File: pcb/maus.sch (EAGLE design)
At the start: 87 parts, among them IC1 AD712R, Q1 BSS123, Q2 BSS123, Q3 BSS123, Q4 BSS123, Q5 BSS123, U1 ESP32-S2-WROOM, U2 CH340C, U3 CP2102, U4 LP3965EMP-3.3, U5 LSM9DS1TR

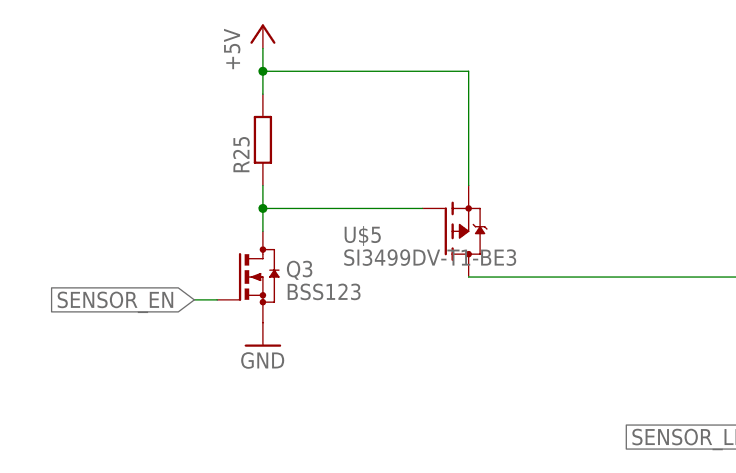
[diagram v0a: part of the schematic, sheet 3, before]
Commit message: fixed mosfet part prefix
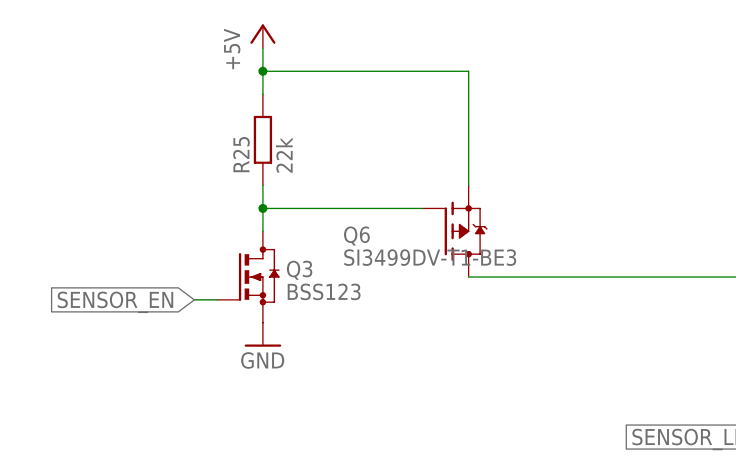
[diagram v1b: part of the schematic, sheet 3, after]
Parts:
- removed U$5, U$6: SI3499DV-T1-BE3, mosfet:SI3499DV-T1-BE3
- added Q6, Q7: SI3499DV-T1-BE3, mosfet:SI3499DV-T1-BE3
- R25: value (none) -> 22k
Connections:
- net +5V: now also Q6.S, Q7.S; no longer U$5.S, U$6.S
- net /VBUS_EN: now also Q7.G; no longer U$6.G
- net N$2: now also Q6.G; no longer U$5.G
- net N$7: now also Q6.D; no longer U$5.D
- net USB_VBUS: now also Q7.D; no longer U$6.D
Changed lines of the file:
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@@
 <part name="Q5" library="transistor-small-signal" library_urn="urn:adsk.eagle:library:401" deviceset="BSS123" device="" package3d_urn="urn:adsk.eagle:package:28738/2"/>
 <part name="JP5" library="pinhead" library_urn="urn:adsk.eagle:library:325" deviceset="PINHD-1X10" device="" package3d_urn="urn:adsk.eagle:package:22406/2"/>
-<part name="U$5" library="mosfet" deviceset="SI3499DV-T1-BE3" device="" package3d_urn="urn:adsk.eagle:package:33743404/1"/>
-<part name="U$6" library="mosfet" deviceset="SI3499DV-T1-BE3" device="" package3d_urn="urn:adsk.eagle:package:33743404/1"/>
 <part name="Q3" library="transistor-small-signal" library_urn="urn:adsk.eagle:library:401" deviceset="BSS123" device="" package3d_urn="urn:adsk.eagle:package:28738/2"/>
-<part name="R25" library="rcl" library_urn="urn:adsk.eagle:library:334" deviceset="R-EU_" device="R0805" package3d_urn="urn:adsk.eagle:package:23553/2"/>
+<part name="R25" library="rcl" library_urn="urn:adsk.eagle:library:334" deviceset="R-EU_" device="R0805" package3d_urn="urn:adsk.eagle:package:23553/2" value="22k"/>
 <part name="GND41" library="supply1" library_urn="urn:adsk.eagle:library:371" deviceset="GND" device=""/>
+<part name="Q6" library="mosfet" deviceset="SI3499DV-T1-BE3" device="" package3d_urn="urn:adsk.eagle:package:33743404/1"/>
+<part name="Q7" library="mosfet" deviceset="SI3499DV-T1-BE3" device="" package3d_urn="urn:adsk.eagle:package:33743404/1"/>
 </parts>
 <sheets>
@@
 <attribute name="VALUE" x="38.1" y="121.92" size="1.778" layer="96" rot="R90"/>
 </instance>
-<instance part="U$5" gate="T$1" x="60.96" y="104.14" smashed="yes">
-<attribute name="VALUE" x="49.53" y="100.33" size="1.778" layer="96"/>
-<attribute name="NAME" x="49.53" y="102.87" size="1.778" layer="95"/>
-</instance>
 <instance part="Q3" gate="G$1" x="40.64" y="99.06" smashed="yes">
 <attribute name="NAME" x="43.18" y="99.06" size="1.778" layer="95"/>
@@
 <instance part="GND41" gate="1" x="40.64" y="91.44" smashed="yes">
 <attribute name="VALUE" x="38.1" y="88.9" size="1.778" layer="96"/>
+</instance>
+<instance part="Q6" gate="G$1" x="60.96" y="104.14" smashed="yes">
+<attribute name="VALUE" x="49.53" y="100.33" size="1.778" layer="96"/>
+<attribute name="NAME" x="49.53" y="102.87" size="1.778" layer="95"/>
 </instance>
 </instances>
@@
 <wire x1="165.1" y1="58.42" x2="165.1" y2="66.04" width="0.1524" layer="91"/>
 <wire x1="165.1" y1="66.04" x2="182.88" y2="66.04" width="0.1524" layer="91"/>
-<pinref part="U$5" gate="T$1" pin="D"/>
+<pinref part="Q6" gate="G$1" pin="D"/>
 </segment>
 </net>
@@
 <pinref part="R25" gate="G$1" pin="2"/>
 <wire x1="40.64" y1="124.46" x2="40.64" y2="121.92" width="0.1524" layer="91"/>
-<pinref part="U$5" gate="T$1" pin="S"/>
 <wire x1="40.64" y1="121.92" x2="40.64" y2="119.38" width="0.1524" layer="91"/>
 <wire x1="40.64" y1="121.92" x2="63.5" y2="121.92" width="0.1524" layer="91"/>
 <wire x1="63.5" y1="121.92" x2="63.5" y2="109.22" width="0.1524" layer="91"/>
 <junction x="40.64" y="121.92"/>
+<pinref part="Q6" gate="G$1" pin="S"/>
 </segment>
 </net>
@@
 <pinref part="Q3" gate="G$1" pin="D"/>
 <wire x1="40.64" y1="109.22" x2="40.64" y2="106.68" width="0.1524" layer="91"/>
-<pinref part="U$5" gate="T$1" pin="G"/>
 <wire x1="40.64" y1="106.68" x2="40.64" y2="104.14" width="0.1524" layer="91"/>
 <wire x1="40.64" y1="106.68" x2="58.42" y2="106.68" width="0.1524" layer="91"/>
 <junction x="40.64" y="106.68"/>
+<pinref part="Q6" gate="G$1" pin="G"/>
 </segment>
 </net>
@@
 <attribute name="VALUE" x="236.22" y="58.42" size="1.778" layer="96"/>
 </instance>
-<instance part="U$6" gate="T$1" x="96.52" y="96.52" smashed="yes" rot="R270">
+<instance part="Q7" gate="G$1" x="96.52" y="96.52" smashed="yes" rot="R270">
 <attribute name="VALUE" x="92.71" y="107.95" size="1.778" layer="96" rot="R270"/>
 <attribute name="NAME" x="95.25" y="107.95" size="1.778" layer="95" rot="R270"/>
@@
 <wire x1="101.6" y1="93.98" x2="111.76" y2="93.98" width="0.1524" layer="91"/>
 <wire x1="111.76" y1="93.98" x2="111.76" y2="96.52" width="0.1524" layer="91"/>
-<pinref part="U$6" gate="T$1" pin="S"/>
+<pinref part="Q7" gate="G$1" pin="S"/>
 </segment>
 <segment>
@@
 <wire x1="99.06" y1="119.38" x2="99.06" y2="99.06" width="0.1524" layer="91"/>
 <label x="88.9" y="119.38" size="1.778" layer="95"/>
-<pinref part="U$6" gate="T$1" pin="G"/>
+<pinref part="Q7" gate="G$1" pin="G"/>
 </segment>
 <segment>
@@
 <wire x1="91.44" y1="93.98" x2="66.04" y2="93.98" width="0.1524" layer="91"/>
 <label x="66.04" y="93.98" size="1.778" layer="95"/>
-<pinref part="U$6" gate="T$1" pin="D"/>
-</segment>
-</net>
+<pinref part="Q7" gate="G$1" pin="D"/>
+</segment>
+</net>

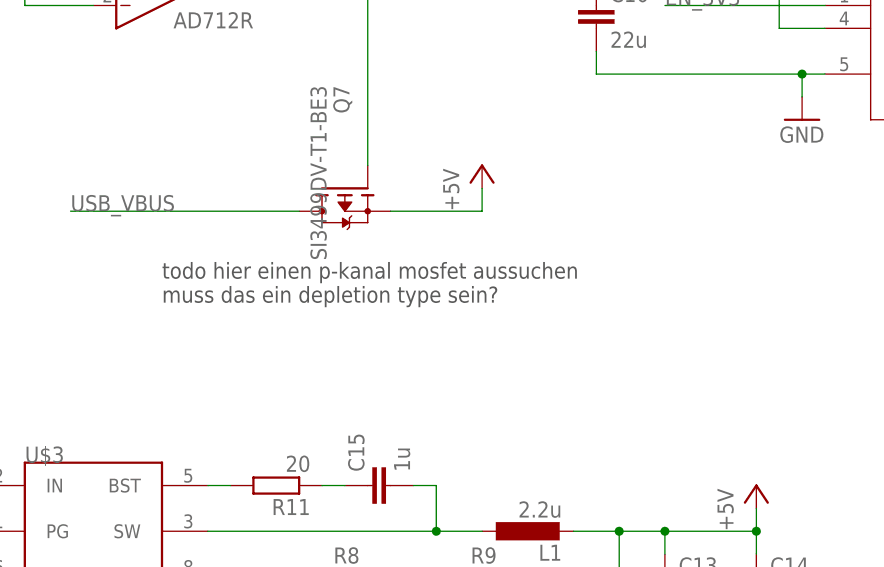
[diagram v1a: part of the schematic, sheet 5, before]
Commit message: removed note about mosfet in power schematic. close #14
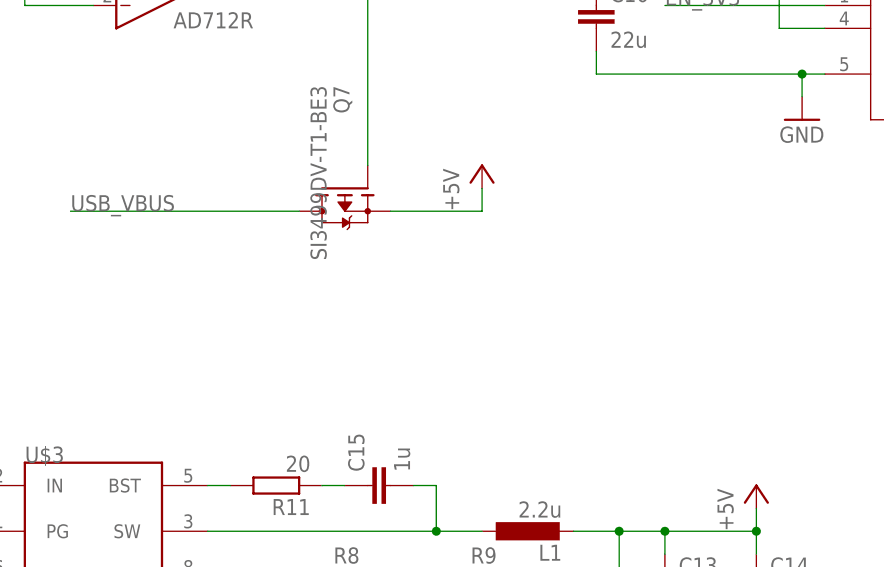
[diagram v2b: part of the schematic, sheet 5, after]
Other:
- note removed: "todo hier einen p-kanal mosfet aussuchen muss das ein depletion type sein?"
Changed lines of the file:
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@@
 <description>description</description>
 <plain>
-<text x="76.2" y="83.82" size="1.778" layer="97">todo hier einen p-kanal mosfet aussuchen
-muss das ein depletion type sein?</text>
 <text x="251.46" y="50.8" size="1.778" layer="97">es soll die 3v3-Leitung an gehen, wenn das Gerät über USB
 (VBUS_EN) betrieben wird oder der Buck stabil ist (PGOOD)

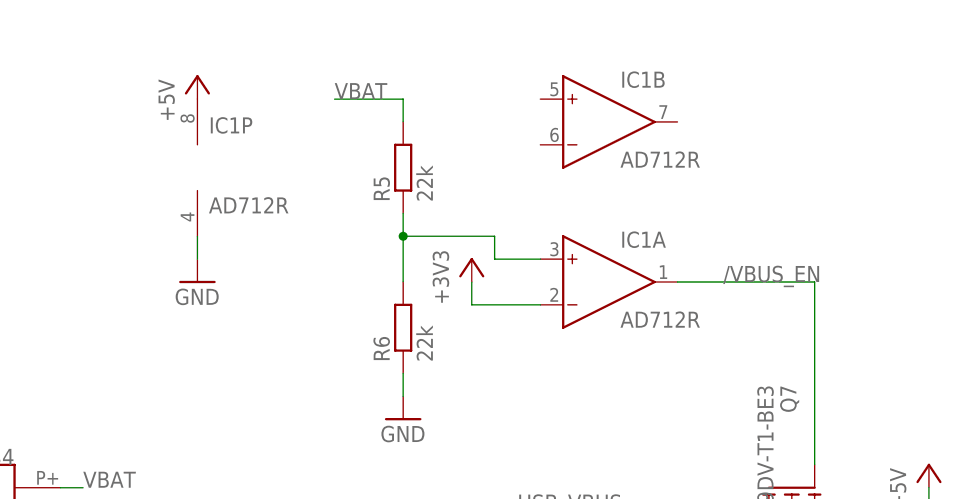
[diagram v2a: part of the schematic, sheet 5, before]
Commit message: now uses LM358DR opamp
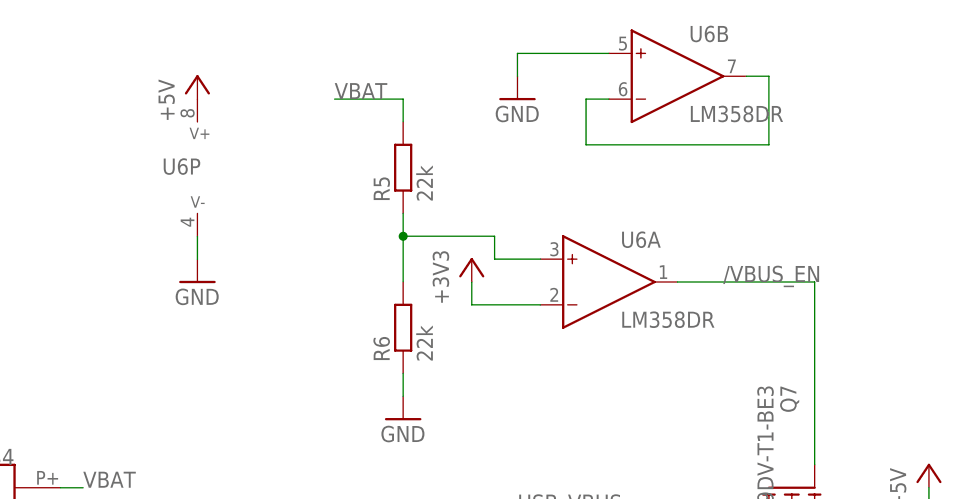
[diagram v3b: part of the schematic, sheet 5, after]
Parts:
- removed IC1: AD712R, analog-devices:AD712R
- added U6: LM358DR, LM358DR:LM358DR
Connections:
- new net N$9: U6B.IN-, U6B.OUT
- net +3V3: now also U6A.IN-; no longer IC1A.IN-
- net +5V: now also U6P.V+; no longer IC1P.V+
- net /VBUS_EN: now also U6A.OUT; no longer IC1A.OUT
- net GND: now also U6B.IN+, U6P.V-; no longer IC1P.V-
- net N$13: now also U6A.IN+; no longer IC1A.IN+
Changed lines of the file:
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@@
 <part name="C8" library="rcl" library_urn="urn:adsk.eagle:library:334" deviceset="C-EU" device="C0805" package3d_urn="urn:adsk.eagle:package:23617/2" value="100nF"/>
 <part name="C9" library="rcl" library_urn="urn:adsk.eagle:library:334" deviceset="C-EU" device="C0805" package3d_urn="urn:adsk.eagle:package:23617/2" value="100nF"/>
-<part name="IC1" library="analog-devices" library_urn="urn:adsk.eagle:library:102" deviceset="AD712" device="R" package3d_urn="urn:adsk.eagle:package:30987/2"/>
 <part name="P+2" library="supply1" library_urn="urn:adsk.eagle:library:371" deviceset="+5V" device=""/>
 <part name="P+3" library="supply1" library_urn="urn:adsk.eagle:library:371" deviceset="+5V" device=""/>
@@
 <part name="Q6" library="mosfet" deviceset="SI3499DV-T1-BE3" device="" package3d_urn="urn:adsk.eagle:package:33743404/1"/>
 <part name="Q7" library="mosfet" deviceset="SI3499DV-T1-BE3" device="" package3d_urn="urn:adsk.eagle:package:33743404/1"/>
+<part name="U6" library="LM358DR" deviceset="LM358DR" device="" package3d_urn="urn:adsk.eagle:package:33744331/1"/>
+<part name="GND42" library="supply1" library_urn="urn:adsk.eagle:library:371" deviceset="GND" device=""/>
 </parts>
 <sheets>
@@
 </plain>
 <instances>
-<instance part="IC1" gate="A" x="73.66" y="119.38" smashed="yes">
-<attribute name="NAME" x="77.47" y="123.19" size="1.778" layer="95"/>
-<attribute name="VALUE" x="77.47" y="114.3" size="1.778" layer="96"/>
-</instance>
-<instance part="IC1" gate="B" x="73.66" y="137.16" smashed="yes">
-<attribute name="NAME" x="77.47" y="140.97" size="1.778" layer="95"/>
-<attribute name="VALUE" x="77.47" y="132.08" size="1.778" layer="96"/>
-</instance>
-<instance part="IC1" gate="P" x="30.48" y="132.08" smashed="yes">
-<attribute name="NAME" x="31.75" y="135.89" size="1.778" layer="95"/>
-<attribute name="VALUE" x="31.75" y="127" size="1.778" layer="96"/>
-</instance>
 <instance part="P+2" gate="1" x="30.48" y="142.24" smashed="yes">
 <attribute name="VALUE" x="27.94" y="137.16" size="1.778" layer="96" rot="R90"/>
@@
 <attribute name="VALUE" x="92.71" y="107.95" size="1.778" layer="96" rot="R270"/>
 <attribute name="NAME" x="95.25" y="107.95" size="1.778" layer="95" rot="R270"/>
+</instance>
+<instance part="U6" gate="A" x="73.66" y="119.38" smashed="yes">
+<attribute name="NAME" x="77.47" y="123.19" size="1.778" layer="95"/>
+<attribute name="VALUE" x="77.47" y="114.3" size="1.778" layer="96"/>
+</instance>
+<instance part="U6" gate="P" x="30.48" y="132.08" smashed="yes">
+<attribute name="NAME" x="26.543" y="131.318" size="1.778" layer="95"/>
+</instance>
+<instance part="U6" gate="B" x="81.28" y="142.24" smashed="yes">
+<attribute name="NAME" x="85.09" y="146.05" size="1.778" layer="95"/>
+<attribute name="VALUE" x="85.09" y="137.16" size="1.778" layer="96"/>
+</instance>
+<instance part="GND42" gate="1" x="66.04" y="139.7" smashed="yes">
+<attribute name="VALUE" x="63.5" y="137.16" size="1.778" layer="96"/>
 </instance>
 </instances>
@@
 </segment>
 <segment>
-<pinref part="IC1" gate="P" pin="V-"/>
 <wire x1="30.48" y1="121.92" x2="30.48" y2="124.46" width="0.1524" layer="91"/>
 <pinref part="GND3" gate="1" pin="GND"/>
+<pinref part="U6" gate="P" pin="V-"/>
 </segment>
 <segment>
@@
 <wire x1="17.78" y1="86.36" x2="17.78" y2="83.82" width="0.1524" layer="91"/>
 </segment>
+<segment>
+<pinref part="GND42" gate="1" pin="GND"/>
+<pinref part="U6" gate="B" pin="IN+"/>
+<wire x1="66.04" y1="142.24" x2="66.04" y2="144.78" width="0.1524" layer="91"/>
+<wire x1="66.04" y1="144.78" x2="76.2" y2="144.78" width="0.1524" layer="91"/>
+</segment>
 </net>
 <net name="+5V" class="0">
-<segment>
-<pinref part="IC1" gate="P" pin="V+"/>
-<pinref part="P+2" gate="1" pin="+5V"/>
-</segment>
 <segment>
 <pinref part="P+3" gate="1" pin="+5V"/>
@@
 <pinref part="P+6" gate="1" pin="+5V"/>
 </segment>
+<segment>
+<pinref part="P+2" gate="1" pin="+5V"/>
+<pinref part="U6" gate="P" pin="V+"/>
+</segment>
 </net>
 <net name="/VBUS_EN" class="0">
 <segment>
-<pinref part="IC1" gate="A" pin="OUT"/>
 <wire x1="83.82" y1="119.38" x2="99.06" y2="119.38" width="0.1524" layer="91"/>
 <wire x1="99.06" y1="119.38" x2="99.06" y2="99.06" width="0.1524" layer="91"/>
 <label x="88.9" y="119.38" size="1.778" layer="95"/>
 <pinref part="Q7" gate="G$1" pin="G"/>
+<pinref part="U6" gate="A" pin="OUT"/>
 </segment>
 <segment>
@@
 <segment>
 <pinref part="+3V2" gate="G$1" pin="+3V3"/>
-<pinref part="IC1" gate="A" pin="IN-"/>
 <wire x1="60.96" y1="119.38" x2="60.96" y2="116.84" width="0.1524" layer="91"/>
 <wire x1="60.96" y1="116.84" x2="68.58" y2="116.84" width="0.1524" layer="91"/>
+<pinref part="U6" gate="A" pin="IN-"/>
 </segment>
 <segment>
@@
 <pinref part="R6" gate="G$1" pin="2"/>
 <wire x1="53.34" y1="127" x2="53.34" y2="124.46" width="0.1524" layer="91"/>
-<pinref part="IC1" gate="A" pin="IN+"/>
 <wire x1="53.34" y1="124.46" x2="53.34" y2="119.38" width="0.1524" layer="91"/>
 <wire x1="68.58" y1="121.92" x2="63.5" y2="121.92" width="0.1524" layer="91"/>
@@
 <wire x1="63.5" y1="124.46" x2="53.34" y2="124.46" width="0.1524" layer="91"/>
 <junction x="53.34" y="124.46"/>
+<pinref part="U6" gate="A" pin="IN+"/>
 </segment>
 </net>
@@
 </segment>
 </net>
+<net name="N$9" class="0">
+<segment>
+<pinref part="U6" gate="B" pin="IN-"/>
+<wire x1="76.2" y1="139.7" x2="73.66" y2="139.7" width="0.1524" layer="91"/>
+<wire x1="73.66" y1="139.7" x2="73.66" y2="134.62" width="0.1524" layer="91"/>
+<wire x1="73.66" y1="134.62" x2="93.98" y2="134.62" width="0.1524" layer="91"/>
+<wire x1="93.98" y1="134.62" x2="93.98" y2="142.24" width="0.1524" layer="91"/>
+<pinref part="U6" gate="B" pin="OUT"/>
+<wire x1="93.98" y1="142.24" x2="91.44" y2="142.24" width="0.1524" layer="91"/>
+</segment>
+</net>

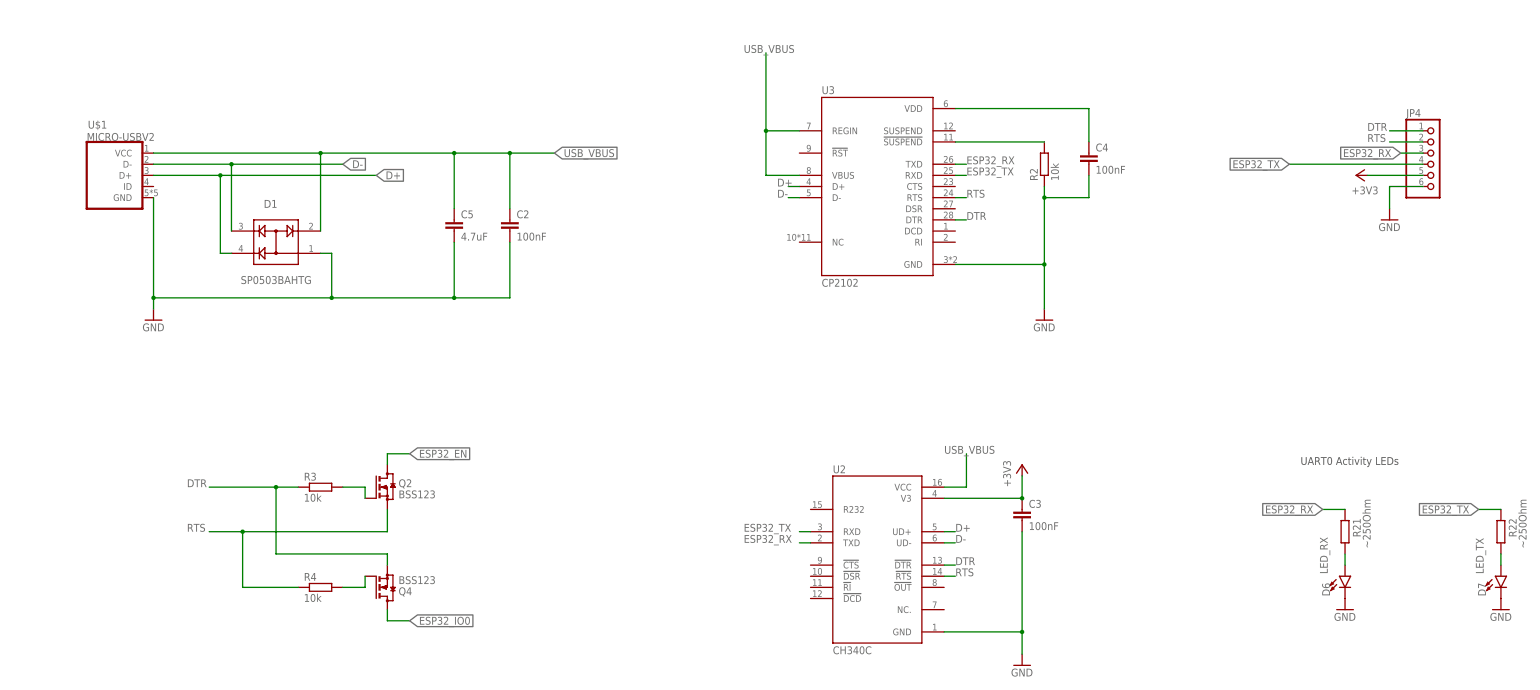
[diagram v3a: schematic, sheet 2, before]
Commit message: fix: self powered CP2102 & CH340C, enable pin voltages ES32
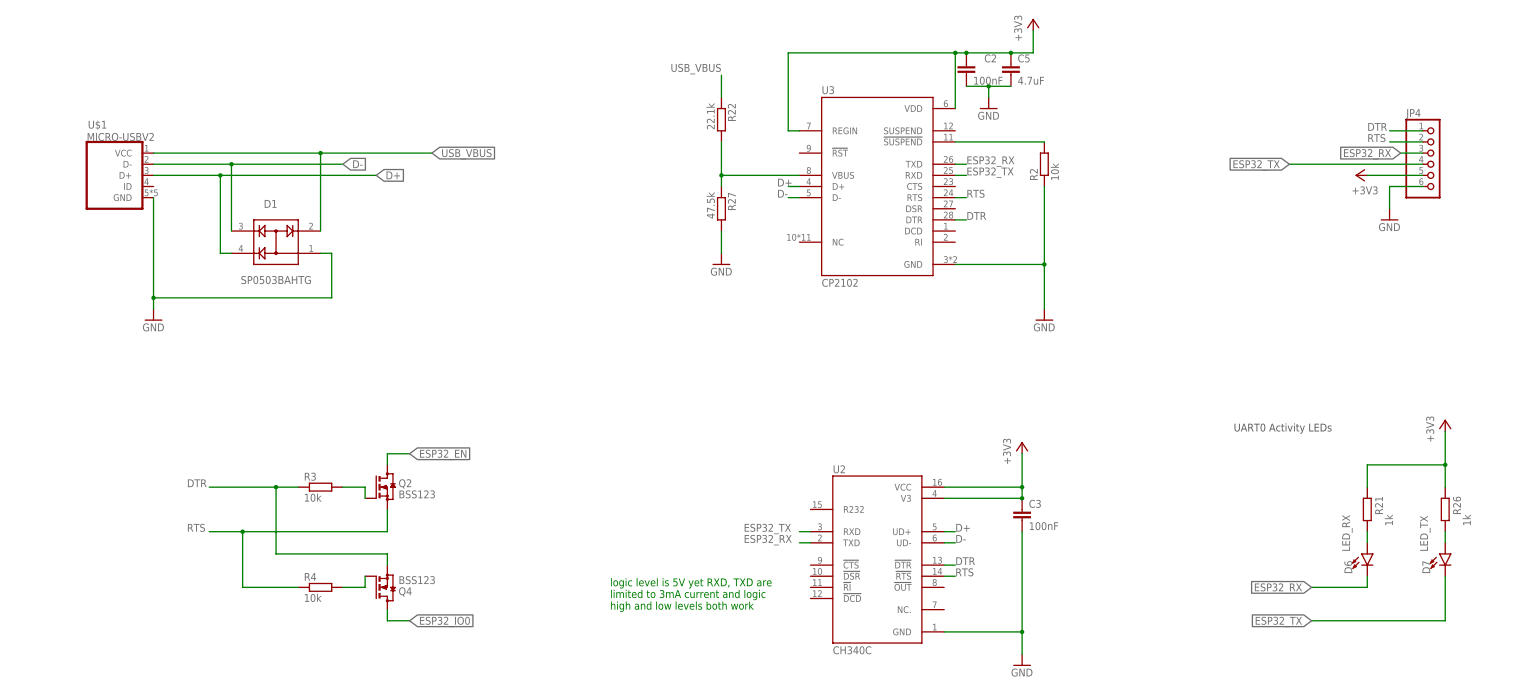
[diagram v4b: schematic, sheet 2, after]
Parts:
- removed C4: 100nF, rcl:C-EUC0805
- added R26: 1k, rcl:R-EU_R0805
- added R27: 47.5k, rcl:R-EU_R0805
- R21: value ~250Ohm -> 1k
- R22: value ~250Ohm -> 22.1k
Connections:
- removed net N$10: D7.A, R22.1
- removed net N$4: C4.1, U3.VDD
- new net N$22: D7.A, R26.1
- net +3V3: now also C2.1, C5.1, R21.2, R23.2, R24.2, R26.2, U2.VCC, U3.REGIN, U3.VDD
- net +5V: no longer R23.2, R24.2
- net ESP32_RX: now also D6.C; no longer R21.2
- net ESP32_TX: now also D7.C; no longer R22.2
- net GND: now also R27.2; no longer C4.2, D6.C, D7.C
- net USB_VBUS: now also R22.1, R22.2, R27.1; no longer C2.1, C5.1, U2.VCC, U3.REGIN
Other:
- note added: "logic level is 5V yet RXD, TXD are limited to 3mA current and logic high and low levels both work"
- moved on the sheet: C2, C5, D6, D7, R21, R22
